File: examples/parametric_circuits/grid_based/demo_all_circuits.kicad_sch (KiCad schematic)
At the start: 15 parts, among them J2 SWD, U1 LM7805, U3 STM32G030K8Tx

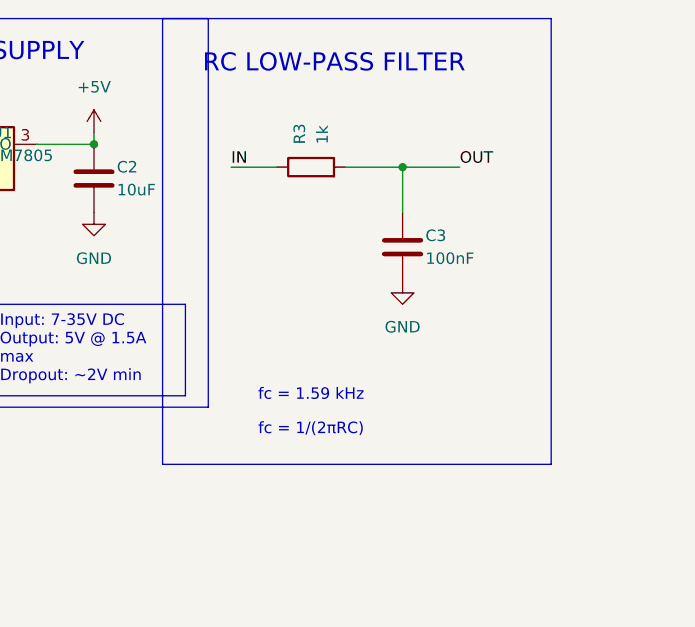
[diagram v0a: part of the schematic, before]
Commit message: Add comprehensive example_circuit.py with parametric circuit patterns
This commit reorganizes examples and adds a single comprehensive example
file demonstrating parametric circuit design with grid-based positioning.

New Features:
- example_circuit.py: Single-file demo with 4 parametric circuits
  - Voltage divider (grid-based positioning)
  - 5V power supply (LM7805)
  - RC low-pass filter (1kHz)
  - STM32G030K8Tx microprocessor with full support circuitry
- Explanatory text box describing STM32 circuit architecture
- All circuits use parametric functions with x/y offset parameters
- Grid-based positioning for clean integer coordinates

Examples Reorganization:
- parametric_circuits/grid_based/ - Integer grid positioning (RECOMMENDED)
- parametric_circuits/mm_based/ - Traditional mm positioning
- basics/ - Getting started examples
- advanced/ - Complex features (hierarchical, routing)
- utilities/ - Helper tools and logging

Key Benefits:
- Reusable circuit blocks that can be placed anywhere
- Grid-based positioning: pos(x_grid, y_grid) with integers
- Clean separation of positioning approaches
- Comprehensive documentation in README files

🤖 Generated with [Claude Code](https://claude.com/claude-code)

Co-Authored-By: Claude <noreply@anthropic.com>
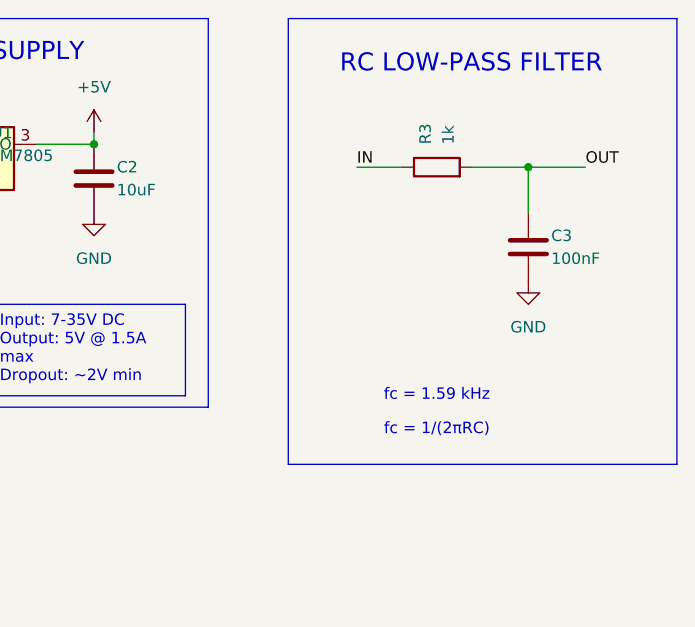
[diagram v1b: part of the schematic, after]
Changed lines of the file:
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@@
 		(instances
 			(project "Demo_All_Circuits"
-				(path "/b70a55c8-25ca-4ccb-b7ea-c33111f91421"
+				(path "/c6091984-9095-4b32-9f00-db38b6361c4f"
 					(reference "R1")
 					(unit 1)
@@
 		(instances
 			(project "Demo_All_Circuits"
-				(path "/b70a55c8-25ca-4ccb-b7ea-c33111f91421"
+				(path "/c6091984-9095-4b32-9f00-db38b6361c4f"
 					(reference "R2")
 					(unit 1)
@@
 		(instances
 			(project "Demo_All_Circuits"
-				(path "/b70a55c8-25ca-4ccb-b7ea-c33111f91421"
+				(path "/c6091984-9095-4b32-9f00-db38b6361c4f"
 					(reference "C1")
 					(unit 1)
@@
 		(instances
 			(project "Demo_All_Circuits"
-				(path "/b70a55c8-25ca-4ccb-b7ea-c33111f91421"
+				(path "/c6091984-9095-4b32-9f00-db38b6361c4f"
 					(reference "U1")
 					(unit 1)
@@
 		(instances
 			(project "Demo_All_Circuits"
-				(path "/b70a55c8-25ca-4ccb-b7ea-c33111f91421"
+				(path "/c6091984-9095-4b32-9f00-db38b6361c4f"
 					(reference "C2")
 					(unit 1)
@@
 		(instances
 			(project "Demo_All_Circuits"
-				(path "/b70a55c8-25ca-4ccb-b7ea-c33111f91421"
+				(path "/c6091984-9095-4b32-9f00-db38b6361c4f"
 					(reference "#PWR01")
 					(unit 1)
@@
 		(instances
 			(project "Demo_All_Circuits"
-				(path "/b70a55c8-25ca-4ccb-b7ea-c33111f91421"
+				(path "/c6091984-9095-4b32-9f00-db38b6361c4f"
 					(reference "#PWR02")
 					(unit 1)
@@
 		(instances
 			(project "Demo_All_Circuits"
-				(path "/b70a55c8-25ca-4ccb-b7ea-c33111f91421"
+				(path "/c6091984-9095-4b32-9f00-db38b6361c4f"
 					(reference "#PWR03")
 					(unit 1)
@@
 		(instances
 			(project "Demo_All_Circuits"
-				(path "/b70a55c8-25ca-4ccb-b7ea-c33111f91421"
+				(path "/c6091984-9095-4b32-9f00-db38b6361c4f"
 					(reference "#PWR04")
 					(unit 1)
@@
 		(instances
 			(project "Demo_All_Circuits"
-				(path "/b70a55c8-25ca-4ccb-b7ea-c33111f91421"
+				(path "/c6091984-9095-4b32-9f00-db38b6361c4f"
 					(reference "#PWR05")
 					(unit 1)
@@
 	(symbol
 		(lib_id "Device:R")
-		(at 127 33.02 90)
+		(at 140.97 33.02 90)
 		(unit 1)
 		(exclude_from_sim no)
@@
 		(fields_autoplaced yes)
 		(property "Reference" "R3"
-			(at 125.7299 30.48 0)
+			(at 139.6999 30.48 0)
 			(effects
 				(font
@@
 		)
 		(property "Value" "1k"
-			(at 128.2699 30.48 0)
+			(at 142.2399 30.48 0)
 			(effects
 				(font
@@
 		(instances
 			(project "Demo_All_Circuits"
-				(path "/b70a55c8-25ca-4ccb-b7ea-c33111f91421"
+				(path "/c6091984-9095-4b32-9f00-db38b6361c4f"
 					(reference "R3")
 					(unit 1)
@@
 	(symbol
 		(lib_id "Device:C")
-		(at 137.16 41.91 0)
+		(at 151.13 41.91 0)
 		(unit 1)
 		(exclude_from_sim no)
@@
 		(fields_autoplaced yes)
 		(property "Reference" "C3"
-			(at 139.7 40.6399 0)
+			(at 153.67 40.6399 0)
 			(effects
 				(font
@@
 		)
 		(property "Value" "100nF"
-			(at 139.7 43.1799 0)
+			(at 153.67 43.1799 0)
 			(effects
 				(font
@@
 		(instances
 			(project "Demo_All_Circuits"
-				(path "/b70a55c8-25ca-4ccb-b7ea-c33111f91421"
+				(path "/c6091984-9095-4b32-9f00-db38b6361c4f"
 					(reference "C3")
 					(unit 1)
@@
 	(symbol
 		(lib_id "power:GND")
-		(at 137.16 45.72 0)
+		(at 151.13 45.72 0)
 		(unit 1)
 		(exclude_from_sim no)
@@
 		(fields_autoplaced yes)
 		(property "Reference" "#PWR06"
-			(at 139.7 44.4499 0)
+			(at 153.67 44.4499 0)
 			(effects
 				(font
@@
 		)
 		(property "Value" "GND"
-			(at 137.16 50.8 0)
-			(effects
-				(font
-					(size 1.27 1.27)
-				)
-			)
-		)
-		(pin "1"
-		)
-		(instances
-			(project "Demo_All_Circuits"
-				(path "/b70a55c8-25ca-4ccb-b7ea-c33111f91421"
+			(at 151.13 50.8 0)
+			(effects
+				(font
+					(size 1.27 1.27)
+				)
+			)
+		)
+		(pin "1"
+		)
+		(instances
+			(project "Demo_All_Circuits"
+				(path "/c6091984-9095-4b32-9f00-db38b6361c4f"
 					(reference "#PWR06")
 					(unit 1)
@@
 		(instances
 			(project "Demo_All_Circuits"
-				(path "/b70a55c8-25ca-4ccb-b7ea-c33111f91421"
+				(path "/c6091984-9095-4b32-9f00-db38b6361c4f"
 					(reference "U3")
 					(unit 1)
@@
 		(instances
 			(project "Demo_All_Circuits"
-				(path "/b70a55c8-25ca-4ccb-b7ea-c33111f91421"
+				(path "/c6091984-9095-4b32-9f00-db38b6361c4f"
 					(reference "R110")
 					(unit 1)
@@
 		(instances
 			(project "Demo_All_Circuits"
-				(path "/b70a55c8-25ca-4ccb-b7ea-c33111f91421"
+				(path "/c6091984-9095-4b32-9f00-db38b6361c4f"
 					(reference "R111")
 					(unit 1)
@@
 		(instances
 			(project "Demo_All_Circuits"
-				(path "/b70a55c8-25ca-4ccb-b7ea-c33111f91421"
+				(path "/c6091984-9095-4b32-9f00-db38b6361c4f"
 					(reference "D110")
 					(unit 1)
@@
 		(instances
 			(project "Demo_All_Circuits"
-				(path "/b70a55c8-25ca-4ccb-b7ea-c33111f91421"
+				(path "/c6091984-9095-4b32-9f00-db38b6361c4f"
 					(reference "C110")
 					(unit 1)
@@
 		(instances
 			(project "Demo_All_Circuits"
-				(path "/b70a55c8-25ca-4ccb-b7ea-c33111f91421"
+				(path "/c6091984-9095-4b32-9f00-db38b6361c4f"
 					(reference "C111")
 					(unit 1)
@@
 		(instances
 			(project "Demo_All_Circuits"
-				(path "/b70a55c8-25ca-4ccb-b7ea-c33111f91421"
+				(path "/c6091984-9095-4b32-9f00-db38b6361c4f"
 					(reference "C112")
 					(unit 1)
@@
 		(instances
 			(project "Demo_All_Circuits"
-				(path "/b70a55c8-25ca-4ccb-b7ea-c33111f91421"
+				(path "/c6091984-9095-4b32-9f00-db38b6361c4f"
 					(reference "J2")
 					(unit 1)
@@
 		(instances
 			(project "Demo_All_Circuits"
-				(path "/b70a55c8-25ca-4ccb-b7ea-c33111f91421"
+				(path "/c6091984-9095-4b32-9f00-db38b6361c4f"
 					(reference "#PWR120")
 					(unit 1)
@@
 		(instances
 			(project "Demo_All_Circuits"
-				(path "/b70a55c8-25ca-4ccb-b7ea-c33111f91421"
+				(path "/c6091984-9095-4b32-9f00-db38b6361c4f"
 					(reference "#PWR121")
 					(unit 1)
@@
 		(instances
 			(project "Demo_All_Circuits"
-				(path "/b70a55c8-25ca-4ccb-b7ea-c33111f91421"
+				(path "/c6091984-9095-4b32-9f00-db38b6361c4f"
 					(reference "#PWR122")
 					(unit 1)
@@
 		(instances
 			(project "Demo_All_Circuits"
-				(path "/b70a55c8-25ca-4ccb-b7ea-c33111f91421"
+				(path "/c6091984-9095-4b32-9f00-db38b6361c4f"
 					(reference "#PWR123")
 					(unit 1)
@@
 		(instances
 			(project "Demo_All_Circuits"
-				(path "/b70a55c8-25ca-4ccb-b7ea-c33111f91421"
+				(path "/c6091984-9095-4b32-9f00-db38b6361c4f"
 					(reference "#PWR124")
 					(unit 1)
@@
 		(instances
 			(project "Demo_All_Circuits"
-				(path "/b70a55c8-25ca-4ccb-b7ea-c33111f91421"
+				(path "/c6091984-9095-4b32-9f00-db38b6361c4f"
 					(reference "#PWR125")
 					(unit 1)
@@
 		(instances
 			(project "Demo_All_Circuits"
-				(path "/b70a55c8-25ca-4ccb-b7ea-c33111f91421"
+				(path "/c6091984-9095-4b32-9f00-db38b6361c4f"
 					(reference "#PWR126")
 					(unit 1)
@@
 		(instances
 			(project "Demo_All_Circuits"
-				(path "/b70a55c8-25ca-4ccb-b7ea-c33111f91421"
+				(path "/c6091984-9095-4b32-9f00-db38b6361c4f"
 					(reference "#PWR127")
 					(unit 1)
@@
 	(wire
 		(pts
-			(xy 118.11 33.02) (xy 123.19 33.02)
-		)
-		(stroke
-			(width 0)
-			(type default)
-		)
-	)
-	(wire
-		(pts
-			(xy 130.81 33.02) (xy 137.16 33.02)
-		)
-		(stroke
-			(width 0)
-			(type default)
-		)
-	)
-	(wire
-		(pts
-			(xy 137.16 33.02) (xy 143.51 33.02)
-		)
-		(stroke
-			(width 0)
-			(type default)
-		)
-	)
-	(wire
-		(pts
-			(xy 137.16 33.02) (xy 137.16 38.1)
-		)
-		(stroke
-			(width 0)
-			(type default)
-		)
-	)
-	(wire
-		(pts
-			(xy 137.16 45.72) (xy 137.16 45.72)
+			(xy 132.08 33.02) (xy 137.16 33.02)
+		)
+		(stroke
+			(width 0)
+			(type default)
+		)
+	)
+	(wire
+		(pts
+			(xy 144.78 33.02) (xy 151.13 33.02)
+		)
+		(stroke
+			(width 0)
+			(type default)
+		)
+	)
+	(wire
+		(pts
+			(xy 151.13 33.02) (xy 157.48 33.02)
+		)
+		(stroke
+			(width 0)
+			(type default)
+		)
+	)
+	(wire
+		(pts
+			(xy 151.13 33.02) (xy 151.13 38.1)
+		)
+		(stroke
+			(width 0)
+			(type default)
+		)
+	)
+	(wire
+		(pts
+			(xy 151.13 45.72) (xy 151.13 45.72)
 		)
 		(stroke
@@
 	)
 	(junction
-		(at 137.16 33.02)
+		(at 151.13 33.02)
 		(diameter 0)
 		(color 0 0 0 0)
@@
 	)
 	(label "IN"
-		(at 118.11 33.02 0)
+		(at 132.08 33.02 0)
 		(effects
 			(font
@@
 	)
 	(label "OUT"
-		(at 143.51 33.02 0)
+		(at 157.48 33.02 0)
 		(effects
 			(font
@@
 	)
 	(rectangle
-		(start 110.49 16.51)
-		(end 153.67 66.04)
+		(start 124.46 16.51)
+		(end 167.64 66.04)
 		(stroke
 			(width 0.127)
@@
 	(text "RC LOW-PASS FILTER"
 		(exclude_from_sim no)
-		(at 129.54 21.59 0.0000)
+		(at 144.78 21.59 0.0000)
 		(effects
 			(font
@@
 	(text "fc = 1.59 kHz"
 		(exclude_from_sim no)
-		(at 127 58.42 0.0000)
+		(at 140.97 58.42 0.0000)
 		(effects
 			(font
@@
 	(text "fc = 1/(2πRC)"
 		(exclude_from_sim no)
-		(at 127 62.23 0.0000)
+		(at 140.97 62.23 0.0000)
 		(effects
 			(font
